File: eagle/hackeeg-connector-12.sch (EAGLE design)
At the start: 13 parts

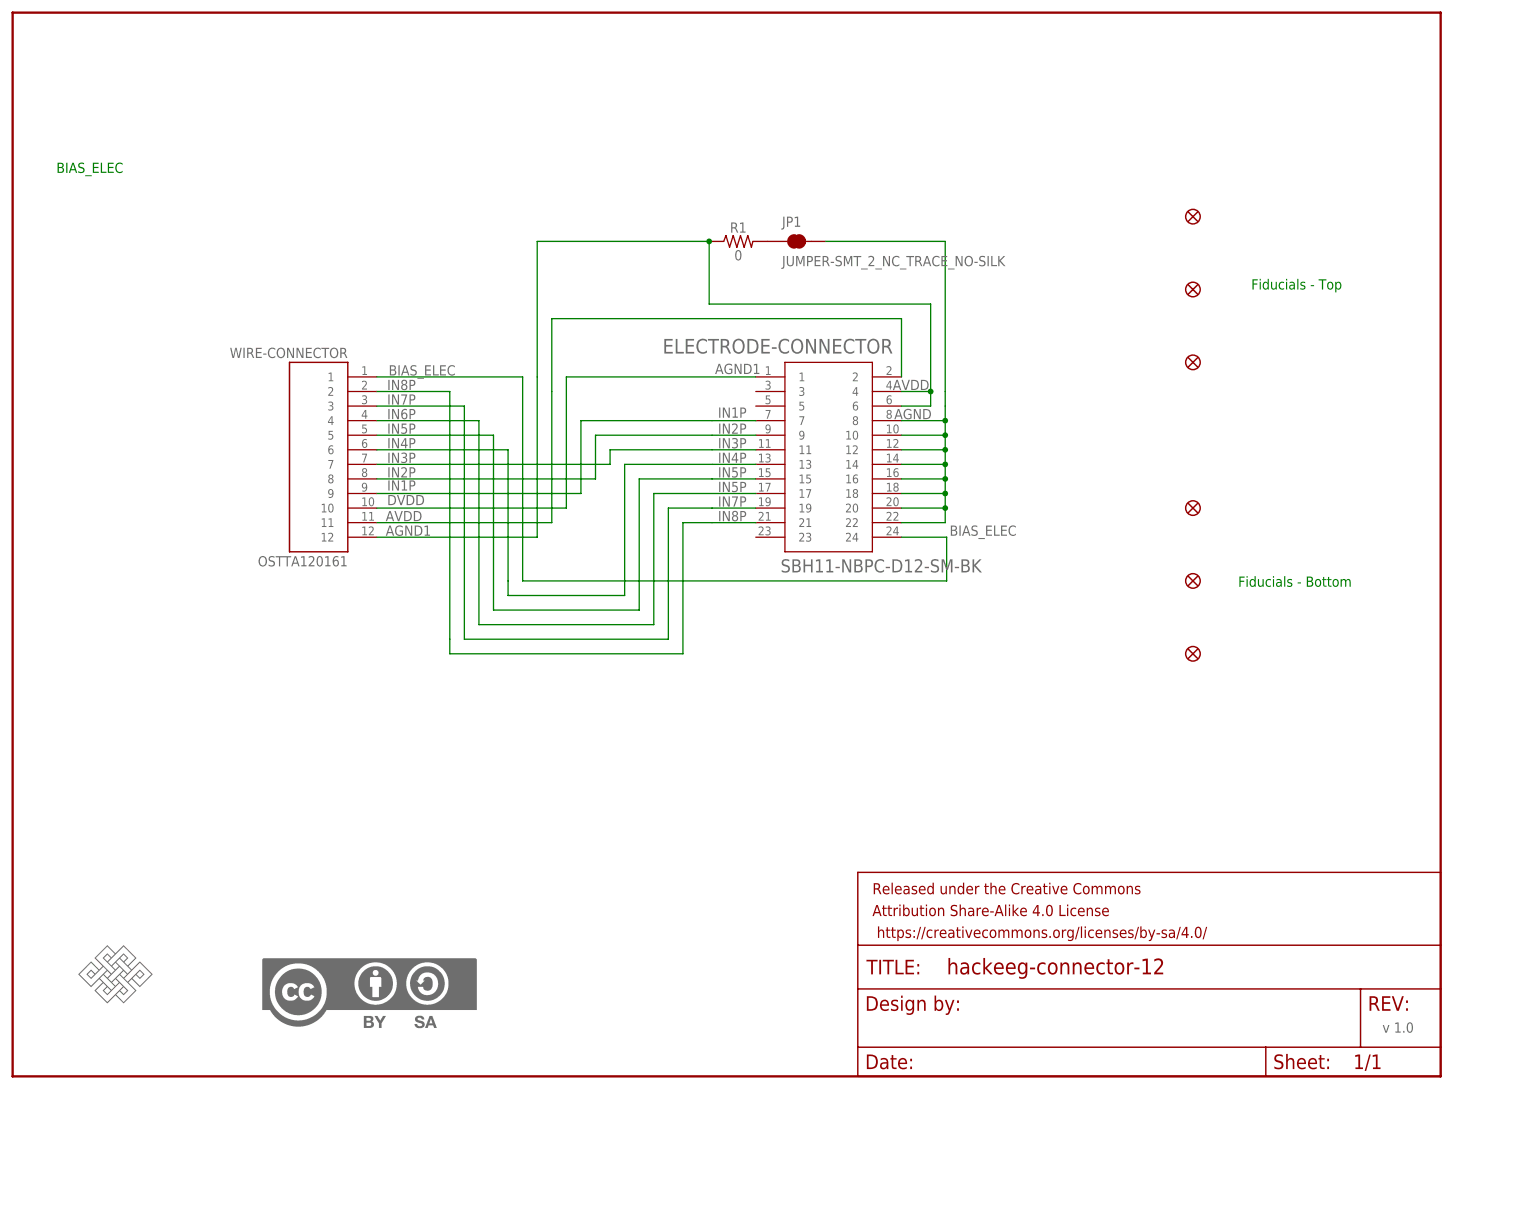
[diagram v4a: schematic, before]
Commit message: relicense to CERN OHL 1.2 - sch and brd
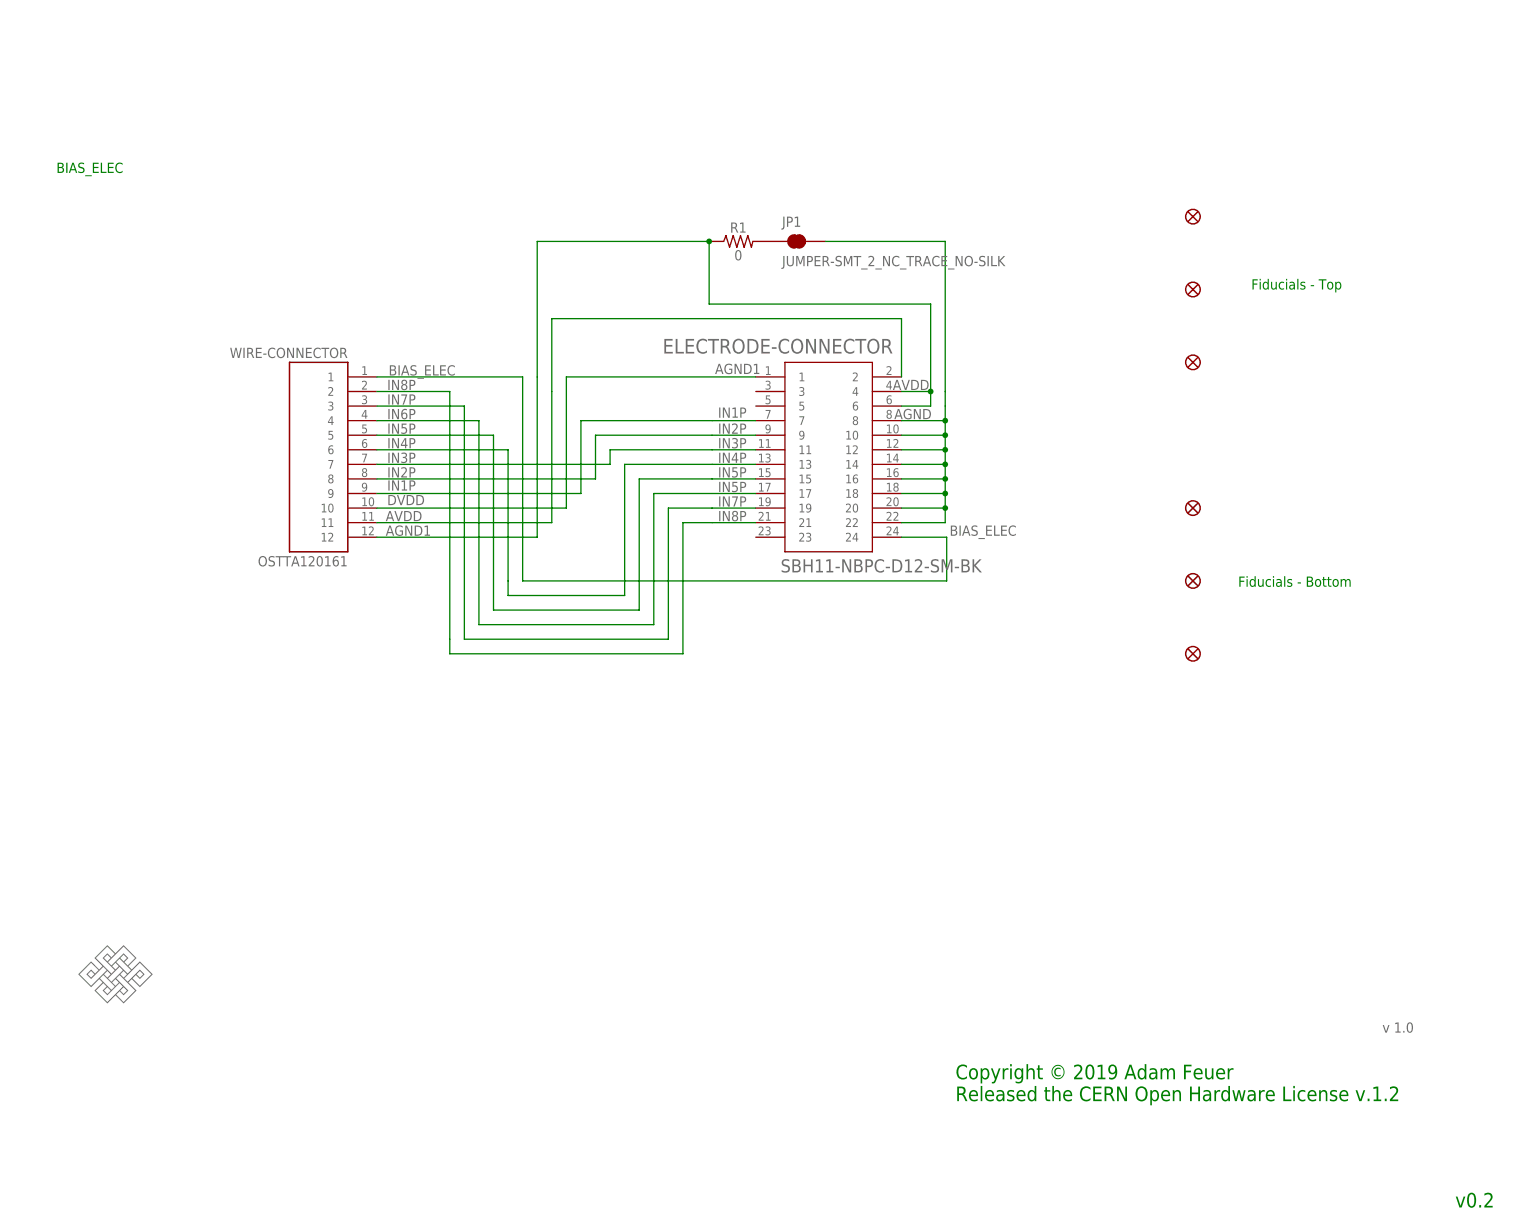
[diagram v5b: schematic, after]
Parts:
- removed FRAME1: FRAME-LETTER, SparkFun-Aesthetics:FRAME-LETTER
- removed U$13: CC-BY-SA, creative-commons:CC-BY-SA
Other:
- note added: "Copyright © 2019 Adam Feuer Released the CERN Open Hardware License v.1.2"
- note added: "v0.2"
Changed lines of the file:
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@@
 </classes>
 <parts>
-<part name="FRAME1" library="SparkFun-Aesthetics" library_urn="urn:adsk.eagle:library:507" deviceset="FRAME-LETTER" device="" package3d_urn="urn:adsk.eagle:package:37121/1"/>
 <part name="ELECTRODE-CONNECTOR" library="SBH11-NBPC-D12-SM-BK" deviceset="SBH11-NBPC-D12-SM-BK" device=""/>
-<part name="U$13" library="creative-commons" deviceset="CC-BY-SA" device=""/>
 <part name="U$1" library="endless-knot" deviceset="ENDLESSKNOT" device="ENDLESSKNOT-MEDIUM"/>
 <part name="FD1" library="SparkFun-Aesthetics" library_urn="urn:adsk.eagle:library:507" deviceset="FIDUCIAL" device="1X2" package3d_urn="urn:adsk.eagle:package:37108/1"/>
@@
 <part name="JP1" library="SparkFun-Jumpers" library_urn="urn:adsk.eagle:library:528" deviceset="JUMPER-SMT_2_NC_TRACE" device="_NO-SILK" package3d_urn="urn:adsk.eagle:package:39286/1"/>
 <part name="WIRE-CONNECTOR" library="OSTTA120161" deviceset="OSTTA120161" device=""/>
+<part name="FRAME1" library="frames" library_urn="urn:adsk.eagle:library:229" deviceset="FRAME_A_L" device="" value="hackeeg-connector-12"/>
 </parts>
 <sheets>
@@
 <text x="303.276" y="165.354" size="1.778" layer="95">AVDD</text>
 <text x="388.62" y="53.34" size="1.778" layer="95">v 1.0</text>
+<text x="401.32" y="22.86" size="2.54" layer="91">v0.2</text>
+<text x="314.198" y="41.402" size="2.54" layer="91">Copyright © 2019 Adam Feuer
+Released the CERN Open Hardware License v.1.2</text>
 </plain>
 <instances>
-<instance part="FRAME1" gate="G$1" x="149.86" y="45.72" smashed="yes"/>
-<instance part="FRAME1" gate="V" x="297.18" y="45.72" smashed="yes">
-<attribute name="LAST_DATE_TIME" x="309.88" y="46.99" size="2.54" layer="94" font="vector"/>
-<attribute name="SHEET" x="383.54" y="46.99" size="2.54" layer="94" font="vector"/>
-<attribute name="DRAWING_NAME" x="312.674" y="63.5" size="2.7432" layer="94" font="vector"/>
-</instance>
 <instance part="ELECTRODE-CONNECTOR" gate="G$1" x="292.1" y="152.4" smashed="yes">
 <attribute name="NAME" x="263.144" y="171.71691875" size="2.54646875" layer="95"/>
 <attribute name="VALUE" x="283.718" y="133.5629" size="2.28846875" layer="96"/>
 </instance>
-<instance part="U$13" gate="G$1" x="193.04" y="53.34" smashed="yes"/>
 <instance part="U$1" gate="G$1" x="167.64" y="63.5" smashed="yes"/>
 <instance part="FD1" gate="G$1" x="355.6" y="170.18" smashed="yes"/>
@@
 <attribute name="NAME" x="208.28" y="170.942" size="1.778" layer="95" rot="MR0"/>
 <attribute name="VALUE" x="208.28" y="134.62" size="1.778" layer="96" rot="MR0"/>
+</instance>
+<instance part="FRAME1" gate="G$1" x="137.16" y="15.24" smashed="yes"/>
+<instance part="FRAME1" gate="G$2" x="309.88" y="15.24" smashed="yes">
+<attribute name="LAST_DATE_TIME" x="322.58" y="16.51" size="2.54" layer="94"/>
+<attribute name="SHEET" x="396.24" y="16.51" size="2.54" layer="94"/>
+<attribute name="DRAWING_NAME" x="327.66" y="34.29" size="2.54" layer="94"/>
 </instance>
 </instances>
@@
 </sheet>
 </sheets>
+<errors>
+</errors>
 </schematic>
 </drawing>
 <compatibility>
+<note version="6.3" minversion="6.2.2" severity="warning">
+Since Version 6.2.2 text objects can contain more than one line,
+which will not be processed correctly with this version.
+</note>
 <note version="8.2" severity="warning">
 Since Version 8.2, EAGLE supports online libraries. The ids
